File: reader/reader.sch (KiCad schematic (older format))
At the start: 58 parts, among them J1 USB_B_Mini, J2 swd, J3 Conn_01x05, J4 v_sup, Q1 CPH3350-TL-W, SW1 SW_Push, U1 BA33BC0FP-E2, U2 ST25R95, U3 STM32G051GxU, U4 FC2004C03-NSWBBW-91*E, Y1 27.12MHz

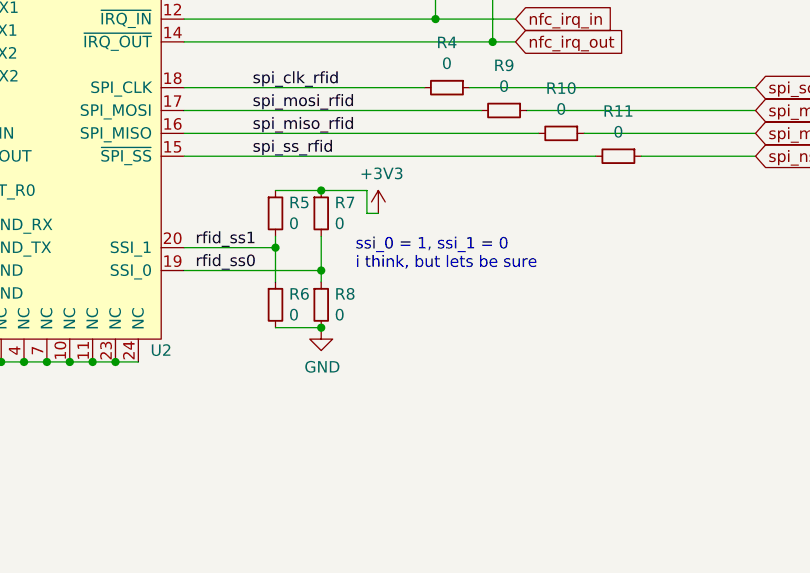
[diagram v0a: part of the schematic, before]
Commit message: Use solder bride instead of 0ohm
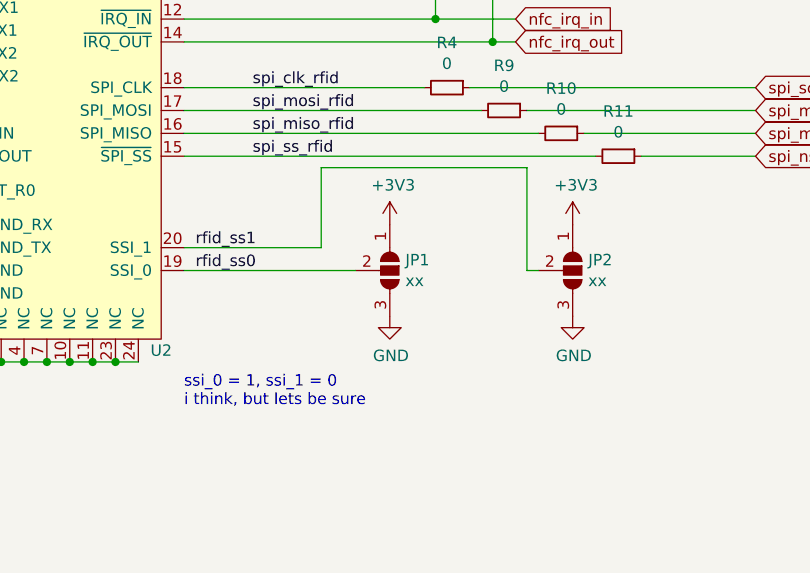
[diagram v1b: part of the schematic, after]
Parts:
- removed R5, R6, R7, R8: 0, Resistor_SMD:R_0603_1608Metric_Pad1.05x0.95mm_HandSolder, symbol Device:R_Small
- added JP1, JP2: xx, Jumper:SolderJumper-3_P1.3mm_Open_RoundedPad1.0x1.5mm, symbol Jumper:SolderJumper_3_Open
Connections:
- net +3V3: now also JP1.1 (A), JP2.1 (A)
- net GND: now also JP1.3 (B), JP2.3 (B)
- net rfid_ss0: now also JP1.2 (C)
- net rfid_ss1: now also JP2.2 (C)
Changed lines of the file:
@@
 	1    0    0    -1
 $EndComp
-$Comp
-L Device:R_Small R5
-U 1 1 61463BAF
-P 8000 4250
-F 0 "R5" H 8059 4296 50  0000 L CNN
-F 1 "0" H 8059 4205 50  0000 L CNN
-F 2 "Resistor_SMD:R_0603_1608Metric_Pad1.05x0.95mm_HandSolder" H 8000 4250 50  0001 C CNN
-F 3 "~" H 8000 4250 50  0001 C CNN
-	1    8000 4250
-	1    0    0    -1
-$EndComp
-$Comp
-L Device:R_Small R7
-U 1 1 614642A8
-P 8200 4250
-F 0 "R7" H 8259 4296 50  0000 L CNN
-F 1 "0" H 8259 4205 50  0000 L CNN
-F 2 "Resistor_SMD:R_0603_1608Metric_Pad1.05x0.95mm_HandSolder" H 8200 4250 50  0001 C CNN
-F 3 "~" H 8200 4250 50  0001 C CNN
-	1    8200 4250
-	1    0    0    -1
-$EndComp
-$Comp
-L Device:R_Small R6
-U 1 1 61464A89
-P 8000 4650
-F 0 "R6" H 8059 4696 50  0000 L CNN
-F 1 "0" H 8059 4605 50  0000 L CNN
-F 2 "Resistor_SMD:R_0603_1608Metric_Pad1.05x0.95mm_HandSolder" H 8000 4650 50  0001 C CNN
-F 3 "~" H 8000 4650 50  0001 C CNN
-	1    8000 4650
-	1    0    0    -1
-$EndComp
-$Comp
-L Device:R_Small R8
-U 1 1 61464A8F
-P 8200 4650
-F 0 "R8" H 8259 4696 50  0000 L CNN
-F 1 "0" H 8259 4605 50  0000 L CNN
-F 2 "Resistor_SMD:R_0603_1608Metric_Pad1.05x0.95mm_HandSolder" H 8200 4650 50  0001 C CNN
-F 3 "~" H 8200 4650 50  0001 C CNN
-	1    8200 4650
-	1    0    0    -1
-$EndComp
-$Comp
-L power:+3V3 #PWR023
-U 1 1 6146EAF9
-P 8450 4250
-F 0 "#PWR023" H 8450 4100 50  0001 C CNN
-F 1 "+3V3" H 8465 4423 50  0000 C CNN
-F 2 "" H 8450 4250 50  0001 C CNN
-F 3 "" H 8450 4250 50  0001 C CNN
-	1    8450 4250
-	1    0    0    -1
-$EndComp
-Wire Wire Line
-	8450 4250 8400 4250
-Wire Wire Line
-	8400 4250 8400 4150
-Wire Wire Line
-	8200 4150 8000 4150
-Wire Wire Line
-	8000 4350 8000 4400
-Wire Wire Line
-	8200 4550 8200 4500
-Wire Wire Line
-	8000 4550 8000 4400
-Connection ~ 8000 4400
-Wire Wire Line
-	8200 4350 8200 4500
-Connection ~ 8200 4500
-Wire Wire Line
-	8000 4750 8200 4750
-$Comp
-L power:GND #PWR021
-U 1 1 614A185E
-P 8200 4750
-F 0 "#PWR021" H 8200 4500 50  0001 C CNN
-F 1 "GND" H 8205 4577 50  0000 C CNN
-F 2 "" H 8200 4750 50  0001 C CNN
-F 3 "" H 8200 4750 50  0001 C CNN
-	1    8200 4750
-	1    0    0    -1
-$EndComp
-Connection ~ 8200 4750
-Text Notes 8350 4500 0    50   ~ 0
+Text Notes 7600 5100 0    50   ~ 0
 ssi_0 = 1, ssi_1 = 0\ni think, but lets be sure
 $Comp
@@
 Text Label 7900 4000 0    50   ~ 0
 spi_ss_rfid
-Wire Wire Line
-	7600 4400 8000 4400
-Wire Wire Line
-	7600 4500 8200 4500
-Text Label 7650 4400 0    50   ~ 0
-rfid_ss1
-Text Label 7650 4500 0    50   ~ 0
-rfid_ss0
 Text Label 5700 3900 0    50   ~ 0
 rfid_xin
@@
 	5250 4400 5250 4750
 Connection ~ 5250 4400
-Connection ~ 8200 4150
-Wire Wire Line
-	8400 4150 8200 4150
 $Comp
 L power:+5V #PWR0106
@@
 Text GLabel 10650 7650 0    50   Input ~ 0
 lcd_d7
+$Comp
+L Jumper:SolderJumper_3_Open JP1
+U 1 1 6168BA39
+P 8500 4500
+F 0 "JP1" V 8454 4568 50  0000 L CNN
+F 1 "xx" V 8545 4568 50  0000 L CNN
+F 2 "Jumper:SolderJumper-3_P1.3mm_Open_RoundedPad1.0x1.5mm" H 8500 4500 50  0001 C CNN
+F 3 "~" H 8500 4500 50  0001 C CNN
+	1    8500 4500
+	0    1    1    0
+$EndComp
+$Comp
+L Jumper:SolderJumper_3_Open JP2
+U 1 1 6168C258
+P 9300 4500
+F 0 "JP2" V 9254 4568 50  0000 L CNN
+F 1 "xx" V 9345 4568 50  0000 L CNN
+F 2 "Jumper:SolderJumper-3_P1.3mm_Open_RoundedPad1.0x1.5mm" H 9300 4500 50  0001 C CNN
+F 3 "~" H 9300 4500 50  0001 C CNN
+	1    9300 4500
+	0    1    1    0
+$EndComp
+$Comp
+L power:+3V3 #PWR0103
+U 1 1 6168D035
+P 8500 4300
+F 0 "#PWR0103" H 8500 4150 50  0001 C CNN
+F 1 "+3V3" H 8515 4473 50  0000 C CNN
+F 2 "" H 8500 4300 50  0001 C CNN
+F 3 "" H 8500 4300 50  0001 C CNN
+	1    8500 4300
+	1    0    0    -1
+$EndComp
+$Comp
+L power:+3V3 #PWR0107
+U 1 1 6168D33A
+P 9300 4300
+F 0 "#PWR0107" H 9300 4150 50  0001 C CNN
+F 1 "+3V3" H 9315 4473 50  0000 C CNN
+F 2 "" H 9300 4300 50  0001 C CNN
+F 3 "" H 9300 4300 50  0001 C CNN
+	1    9300 4300
+	1    0    0    -1
+$EndComp
+$Comp
+L power:GND #PWR0108
+U 1 1 6168D602
+P 8500 4700
+F 0 "#PWR0108" H 8500 4450 50  0001 C CNN
+F 1 "GND" H 8505 4527 50  0000 C CNN
+F 2 "" H 8500 4700 50  0001 C CNN
+F 3 "" H 8500 4700 50  0001 C CNN
+	1    8500 4700
+	1    0    0    -1
+$EndComp
+$Comp
+L power:GND #PWR0109
+U 1 1 6168D868
+P 9300 4700
+F 0 "#PWR0109" H 9300 4450 50  0001 C CNN
+F 1 "GND" H 9305 4527 50  0000 C CNN
+F 2 "" H 9300 4700 50  0001 C CNN
+F 3 "" H 9300 4700 50  0001 C CNN
+	1    9300 4700
+	1    0    0    -1
+$EndComp
+Wire Wire Line
+	8350 4500 7600 4500
+Wire Wire Line
+	9150 4500 9100 4500
+Wire Wire Line
+	9100 4500 9100 4050
+Wire Wire Line
+	9100 4050 8200 4050
+Wire Wire Line
+	8200 4050 8200 4400
+Wire Wire Line
+	8200 4400 7600 4400
+Text Label 7650 4400 0    50   ~ 0
+rfid_ss1
+Text Label 7650 4500 0    50   ~ 0
+rfid_ss0
 $EndSCHEMATC
